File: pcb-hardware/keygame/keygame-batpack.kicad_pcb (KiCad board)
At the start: 2 copper layers, 56 x 84 mm, 18 parts, among them J1 DEBUG_HEADER, J2 POWER_HEADER, J3 Conn_01x04

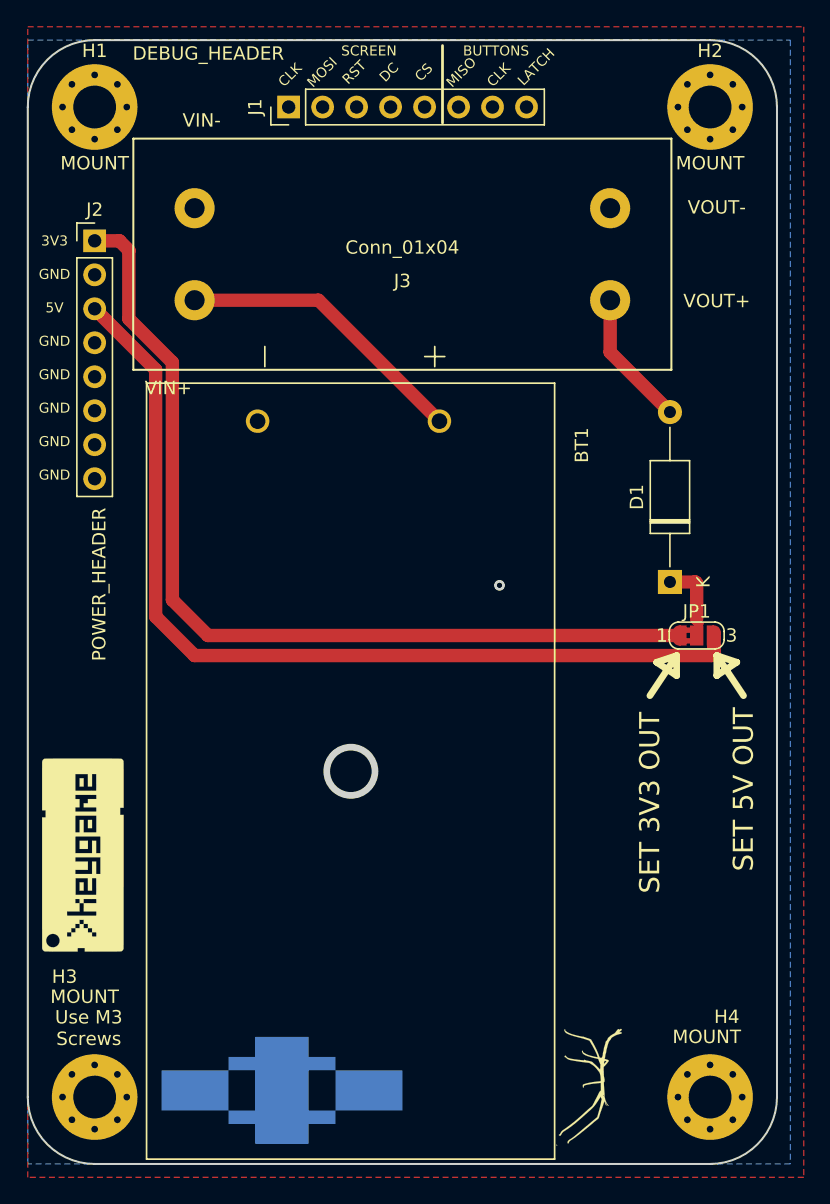
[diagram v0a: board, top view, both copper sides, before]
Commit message: moving to just the RP2040
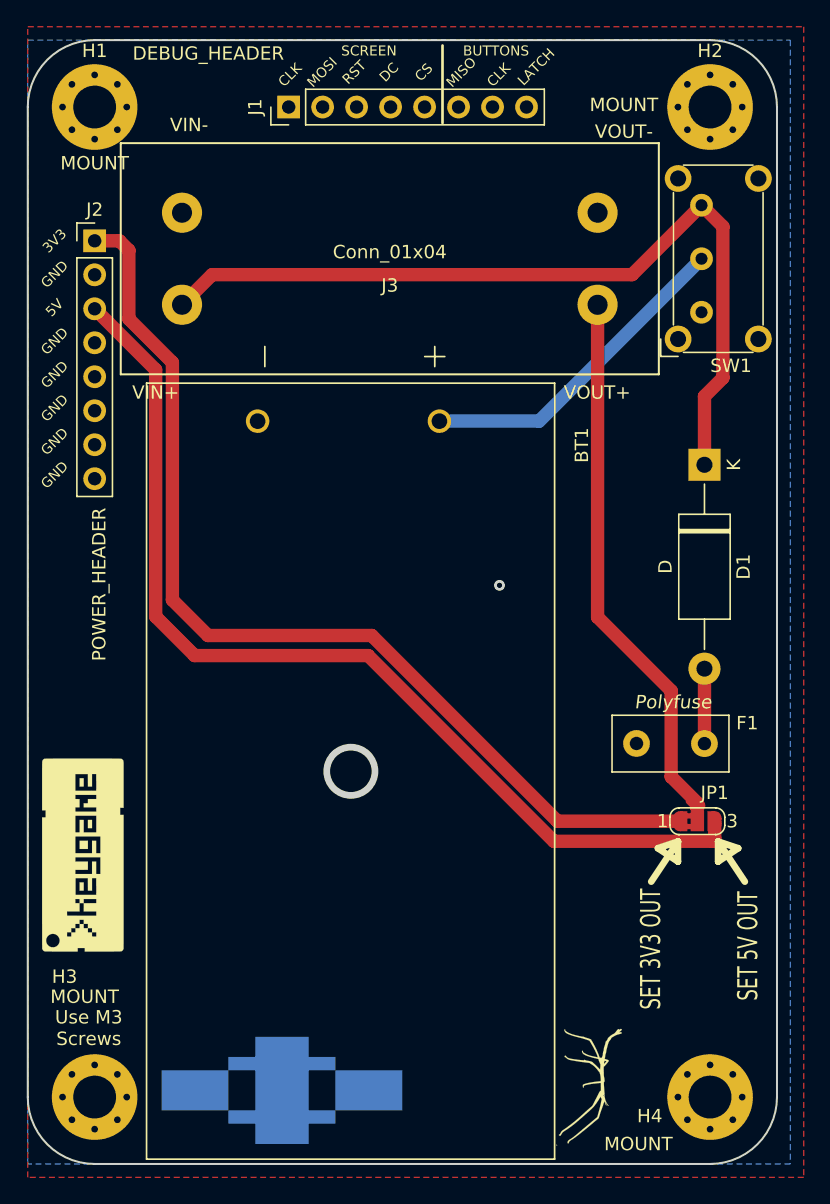
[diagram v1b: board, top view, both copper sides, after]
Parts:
- added F1: Polyfuse, Fuse:Fuse_Littelfuse_395Series, F.Cu at (170.0, 107.2)
- added SW1: SW_SPDT, Button_Switch_THT:SW_E-Switch_EG1224_SPDT_Angled, F.Cu at (169.8, 75.0)
- D1: footprint Diode_THT:D_A-405_P12.70mm_Horizontal -> Diode_THT:D_DO-15_P15.24mm_Horizontal
- moved REF** 56.4 mm to (123.9, 97.9)
- moved JP1 13.9 mm to (169.5, 113.0)
- moved D1 9.13 mm to (170.0, 86.4), turned to 270 degrees
- moved REF** 7.01 mm to (168.3, 122.5)
- moved J3 1.00 mm to (146.5, 71.0)
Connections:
- J3 pad 2: Net-(D1-Pad2) -> Net-(J3-Pad2)
- J3 pad 3: Net-(BT1-Pad1) -> Net-(D1-Pad1)
- JP1 pad 2: Net-(D1-Pad1) -> Net-(J3-Pad2)
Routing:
- net Net-(J3-Pad2): track 0.00 -> 49.5 mm
- net Net-(D1-Pad1): track 13.9 -> 62.5 mm
- net +5V: track 69.2 -> 75.0 mm
- net +3V3: track 69.5 -> 75.3 mm
- net Net-(D1-Pad2): track 10.2 -> 5.60 mm
- net Net-(BT1-Pad1): track 22.0 -> 24.6 mm

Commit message: fixed J4
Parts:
- removed the G*** at (161.5, 132.8)
